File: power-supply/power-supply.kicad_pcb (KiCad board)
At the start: 2 copper layers, 130 x 46.5 mm, 20 parts, among them J1 Barrel_Jack_Switch, J2 Output, U1 LM7812_TO220, U2 LM7912_TO220

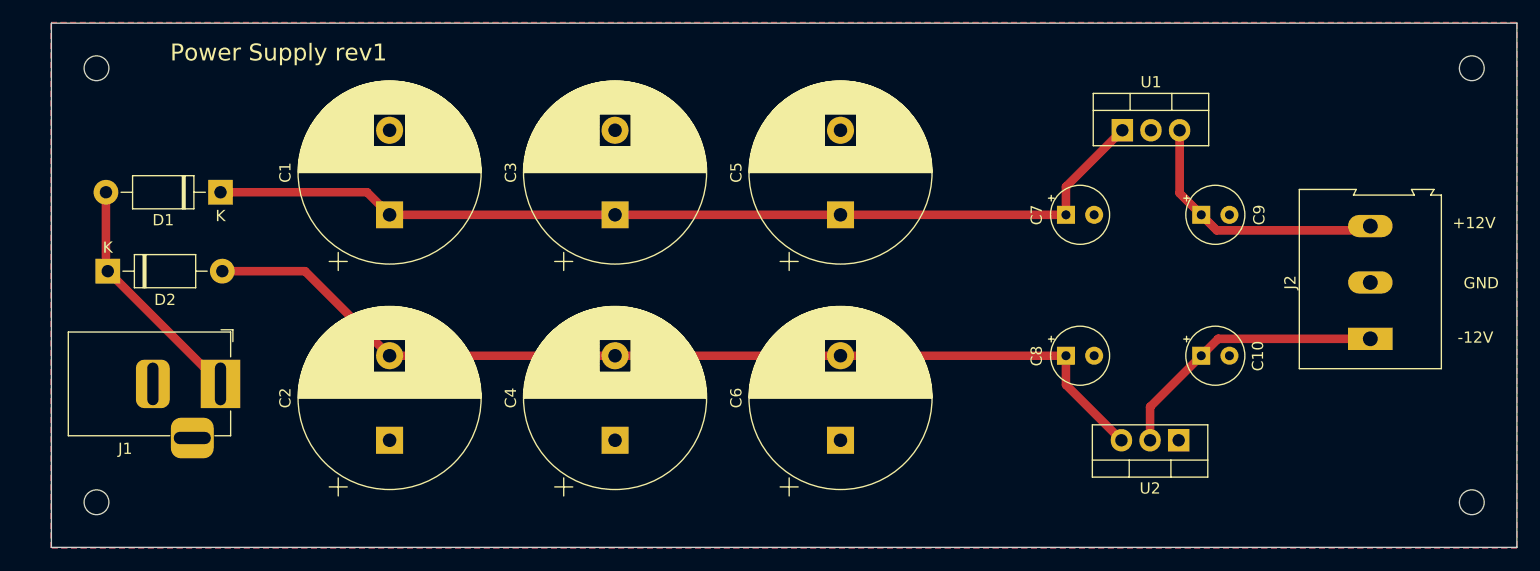
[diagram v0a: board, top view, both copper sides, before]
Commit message: Made mounting holes M3 sized. Generated BOM
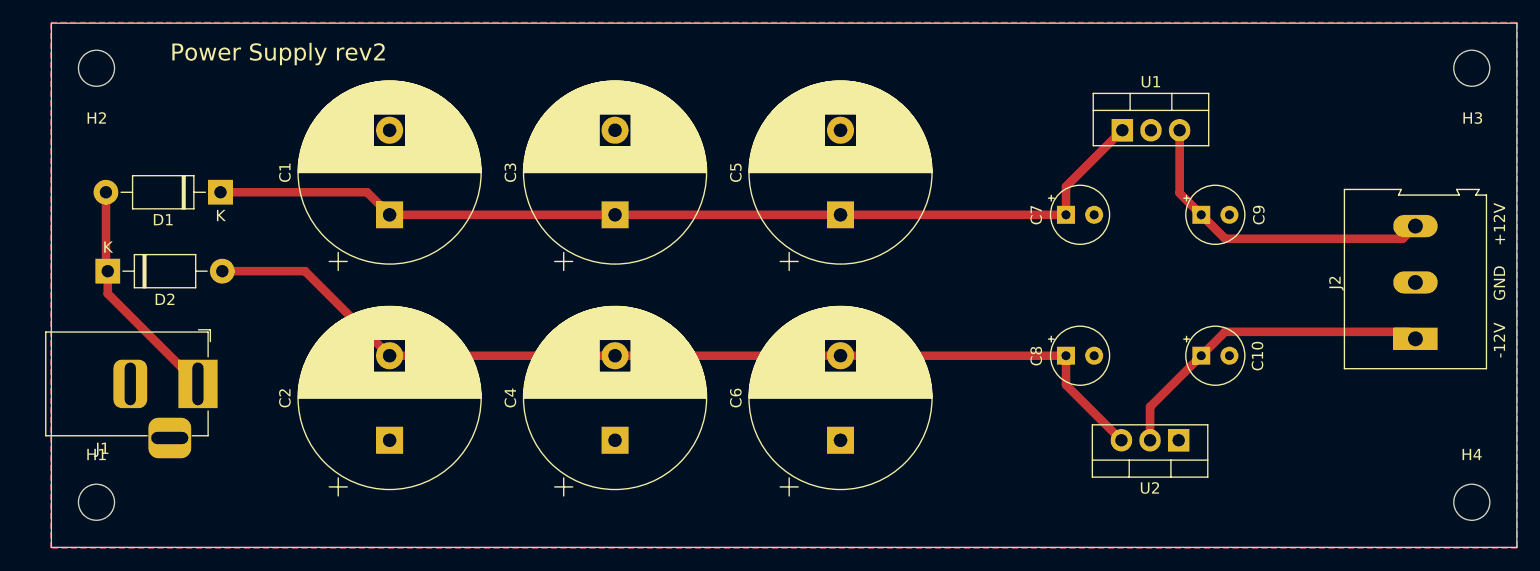
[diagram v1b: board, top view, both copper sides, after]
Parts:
- C2: value 7400uF -> 4700uF
- H1, H3, H4: footprint MountingHole:MountingHole_2.2mm_M2 -> MountingHole:MountingHole_3.2mm_M3
- H2: footprint MountingHole:MountingHole_2.2mm_M2 -> MountingHole:MountingHole_3.2mm_M3; moved to F.Cu
- moved J2 4.00 mm to (206.0, 96.0)
- moved J1 2.00 mm to (98.0, 100.0)
- turned H2 to 0 degrees
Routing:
- net Net-(C9-Pad1): track 24.0 -> 28.6 mm
- net Net-(C10-Pad1): track 25.0 -> 29.5 mm
- net Net-(D1-Pad2): track 21.2 -> 20.4 mm
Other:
- board text added: "Power Supply rev2"
- board text removed: "Power Supply rev1"

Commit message: Updated for rev2
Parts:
- added D3: 1N4007, Diode_THT:D_DO-41_SOD81_P10.16mm_Horizontal, F.Cu at (162.0, 91.2)
- C7: value 1uF -> 0.33uF
- C8: value 1uF -> 2.2uF
- C9: value 1uF -> 0.1uF
- J2: footprint TerminalBlock:TerminalBlock_Altech_AK300-3_P5.00mm -> DEGSON_Screw_Terminals:DG126
- moved H3 25.0 mm to (186.0, 72.0)
- moved H4 25.0 mm to (186.0, 110.5)
- moved J2 22.5 mm to (184.0, 91.2)
- moved C10 15.6 mm to (171.5, 99.0)
- moved C9 15.6 mm to (171.5, 83.5)
- moved U2 13.0 mm to (172.0, 105.0)
- moved U1 12.0 mm to (168.0, 77.5)
- moved C7 10.1 mm to (165.0, 83.5)
- moved C8 10.1 mm to (165.0, 99.0)
- moved C1 5.00 mm to (110.0, 85.0)
- moved C2 5.00 mm to (110.0, 105.0)
- moved C3 5.00 mm to (130.0, 85.0)
- moved C4 5.00 mm to (130.0, 105.0)
- moved C5 5.00 mm to (150.0, 85.0)
- moved C6 5.00 mm to (150.0, 105.0)
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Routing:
- net Net-(C2-Pad2): track 87.5 -> 77.4 mm
- net Net-(C10-Pad1): track 29.5 -> 20.5 mm
- net Net-(C1-Pad1): track 85.4 -> 83.7 mm
- net Net-(C9-Pad1): track 28.6 -> 29.2 mm
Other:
- board size 130 x 46.5 mm -> 105 x 46.5 mm

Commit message: Flipped input/output of 7912
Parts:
- added TP1: TestPoint, TestPoint:TestPoint_Pad_D1.5mm, F.Cu at (161.0, 86.1)
- added TP2: TestPoint, TestPoint:TestPoint_Pad_D1.5mm, F.Cu at (161.0, 104.9)
- moved J1 4.00 mm to (96.0, 96.0)
- moved H1 2.12 mm to (90.5, 109.0)
- moved H2 2.12 mm to (90.5, 73.5)
- moved H3 2.12 mm to (184.5, 73.5)
- moved H4 2.12 mm to (184.5, 109.0)
- moved D2 2.00 mm to (88.0, 88.0)
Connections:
- U2 pad 2: Net-(C10-Pad1) -> Net-(C2-Pad2)
- U2 pad 3: Net-(C2-Pad2) -> Net-(C10-Pad1)
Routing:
- net Net-(C2-Pad2): track 77.4 -> 93.1 mm
- net Net-(C1-Pad1): track 83.7 -> 89.2 mm
- net Net-(D1-Pad2): track 20.4 -> 16.4 mm
- net Net-(C10-Pad1): track 20.5 -> 21.5 mm

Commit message: Added more text detail to PCB
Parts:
- moved TP1 1.11 mm to (161.0, 85.0)
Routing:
- net Net-(C1-Pad1): track 89.2 -> 90.3 mm
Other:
- board text added: "+12"
- board text added: "-12"
- board text added: "12VAC"
- board text added: "Northridge Devices - July 2022"
- board text added: "Power Supply - REV2"
- board text removed: "Power Supply rev2"
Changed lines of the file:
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@@
       (effects (font (size 1 1) (thickness 0.15)))
     )
-    (fp_text value "0.1uF" (at 1.25 3.75) (layer "F.Fab")
+    (fp_text value "0.1uF" (at 1.25 3.75) (layer "F.Fab") hide
       (effects (font (size 1 1) (thickness 0.15)))
     )
@@
       (effects (font (size 1 1) (thickness 0.15)))
     )
-    (fp_text value "LM7812_TO220" (at 2.54 2.5) (layer "F.Fab")
+    (fp_text value "LM7812_TO220" (at 2.54 2.5) (layer "F.Fab") hide
       (effects (font (size 1 1) (thickness 0.15)))
     )
@@
     (property "exclude_from_bom" "")
     (attr exclude_from_pos_files exclude_from_bom)
-    (fp_text reference "H3" (at 0.074 4.454) (layer "Cmts.User")
-      (effects (font (size 1 1) (thickness 0.15)))
-    )
-    (fp_text value "MountingHole" (at -4.498 1.914 90) (layer "F.Fab")
+    (fp_text reference "H3" (at 0.074 4.454) (layer "Cmts.User") hide
+      (effects (font (size 1 1) (thickness 0.15)))
+    )
+    (fp_text value "MountingHole" (at -4.498 1.914 90) (layer "F.Fab") hide
       (effects (font (size 1 1) (thickness 0.15)))
     )
@@
       (effects (font (size 1 1) (thickness 0.15)))
     )
-    (fp_text value "0.33uF" (at 1.25 3.75) (layer "F.Fab")
+    (fp_text value "0.33uF" (at 1.25 3.75) (layer "F.Fab") hide
       (effects (font (size 1 1) (thickness 0.15)))
     )
@@
     (property "exclude_from_bom" "")
     (attr exclude_from_pos_files exclude_from_bom)
-    (fp_text reference "H1" (at 0 -4.2) (layer "Cmts.User")
-      (effects (font (size 1 1) (thickness 0.15)))
-    )
-    (fp_text value "MountingHole" (at 0 4.2) (layer "F.Fab")
+    (fp_text reference "H1" (at 0 -4.2) (layer "Cmts.User") hide
+      (effects (font (size 1 1) (thickness 0.15)))
+    )
+    (fp_text value "MountingHole" (at 0 4.2) (layer "F.Fab") hide
       (effects (font (size 1 1) (thickness 0.15)))
     )
@@
     (property "exclude_from_bom" "")
     (attr exclude_from_pos_files exclude_from_bom)
-    (fp_text reference "H4" (at 0 -4.2) (layer "Cmts.User")
-      (effects (font (size 1 1) (thickness 0.15)))
-    )
-    (fp_text value "MountingHole" (at -5.006 -1.788 90) (layer "F.Fab")
+    (fp_text reference "H4" (at 0 -4.2) (layer "Cmts.User") hide
+      (effects (font (size 1 1) (thickness 0.15)))
+    )
+    (fp_text value "MountingHole" (at -5.006 -1.788 90) (layer "F.Fab") hide
       (effects (font (size 1 1) (thickness 0.15)))
     )
@@
   )
   (footprint "TestPoint:TestPoint_Pad_D1.5mm" (layer "F.Cu")
-    (at 161 86.106)
+    (at 161 85)
     (descr "SMD pad as test Point, diameter 1.5mm")
     (tags "test point SMD pad")
@@
     (property "Sheetname" "")
     (attr exclude_from_pos_files)
-    (fp_text reference "TP1" (at 0 -1.648) (layer "F.SilkS")
+    (fp_text reference "TP1" (at -0.0402 -2.1706) (layer "F.SilkS")
       (effects (font (size 1 1) (thickness 0.15)))
     )
@@
       (effects (font (size 1 1) (thickness 0.15)))
     )
-    (fp_text user "${REFERENCE}" (at 0 -1.65) (layer "F.Fab")
+    (fp_text user "${REFERENCE}" (at 0 -1.65) (layer "F.Fab") hide
       (effects (font (size 1 1) (thickness 0.15)))
     )
@@
       (effects (font (size 1 1) (thickness 0.15)))
     )
-    (fp_text value "LM7912_TO220" (at 2.54 2.5) (layer "F.Fab")
+    (fp_text value "LM7912_TO220" (at 2.54 2.5) (layer "F.Fab") hide
       (effects (font (size 1 1) (thickness 0.15)))
     )
@@
     (property "exclude_from_bom" "")
     (attr exclude_from_pos_files exclude_from_bom)
-    (fp_text reference "H2" (at 0.027 4.454) (layer "Cmts.User")
-      (effects (font (size 1 1) (thickness 0.15)))
-    )
-    (fp_text value "MountingHole" (at 0 4.2) (layer "F.Fab")
+    (fp_text reference "H2" (at 0.027 4.454) (layer "Cmts.User") hide
+      (effects (font (size 1 1) (thickness 0.15)))
+    )
+    (fp_text value "MountingHole" (at 0 4.2) (layer "F.Fab") hide
       (effects (font (size 1 1) (thickness 0.15)))
     )
@@
       (effects (font (size 1 1) (thickness 0.15)))
     )
-    (fp_text value "2.2uF" (at 1.4904 -3.5722) (layer "F.Fab")
+    (fp_text value "2.2uF" (at 1.4904 -3.5722) (layer "F.Fab") hide
       (effects (font (size 1 1) (thickness 0.15)))
     )
@@
       (effects (font (size 1 1) (thickness 0.15)))
     )
-    (fp_text value "1N4007" (at 5.08 2.47) (layer "F.Fab")
+    (fp_text value "1N4007" (at 5.08 2.47) (layer "F.Fab") hide
       (effects (font (size 1 1) (thickness 0.15)))
     )
@@
   )
   (gr_rect (start 85 68) (end 190 114.5) (layer "Edge.Cuts") (width 0.1) (fill none))
+  (gr_text "Northridge Devices - July 2022" (at 164.6174 70.866) (layer "B.SilkS")
+    (effects (font (size 1 1) (thickness 0.15)) (justify mirror))
+  )
   (gr_text "-12V" (at 178.4858 96.1136 90) (layer "F.SilkS")
     (effects (font (size 1 1) (thickness 0.15)))
   )
+  (gr_text "+12" (at 161 87.3) (layer "F.SilkS")
+    (effects (font (size 1 1) (thickness 0.15)))
+  )
   (gr_text "+12V" (at 178.7398 86.2076 90) (layer "F.SilkS")
     (effects (font (size 1 1) (thickness 0.15)))
   )
-  (gr_text "Power Supply rev2" (at 106.8324 70.5612) (layer "F.SilkS")
+  (gr_text "Power Supply - REV2" (at 109.4486 70.866) (layer "F.SilkS")
     (effects (font (size 1.5 1.5) (thickness 0.3)))
+  )
+  (gr_text "12VAC" (at 99.8982 94.3102 270) (layer "F.SilkS")
+    (effects (font (size 1.5 1.5) (thickness 0.2)))
   )
   (gr_text "GND" (at 178.7652 91.059 90) (layer "F.SilkS")
     (effects (font (size 1 1) (thickness 0.15)))
   )
-  (segment (start 162 91.25) (end 162 87.106) (width 0.76) (layer "F.Cu") (net 1))
-  (segment (start 162 87.106) (end 161 86.106) (width 0.76) (layer "F.Cu") (net 1))
+  (gr_text "-12" (at 161 107.3) (layer "F.SilkS")
+    (effects (font (size 1 1) (thickness 0.15)))
+  )
+  (segment (start 162 91.25) (end 162 86) (width 0.76) (layer "F.Cu") (net 1))
+  (segment (start 162 86) (end 161 85) (width 0.76) (layer "F.Cu") (net 1))
   (segment (start 168 77.5) (end 168 80.5) (width 0.76) (layer "B.Cu") (net 1))
   (segment (start 150 85) (end 155.75 85) (width 0.76) (layer "B.Cu") (net 1))
